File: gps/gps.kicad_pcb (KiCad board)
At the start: 2 copper layers, 38 x 38 mm, 32 parts, among them P1 CTL, P2 PWR, P3 UART, U1 USB_A_FEMALE, U2 TXS0102, U3 SE880, U4 ABS25, U5 TPS76318, U6 SGP25C, U7 KT2520, U8 TPS76333

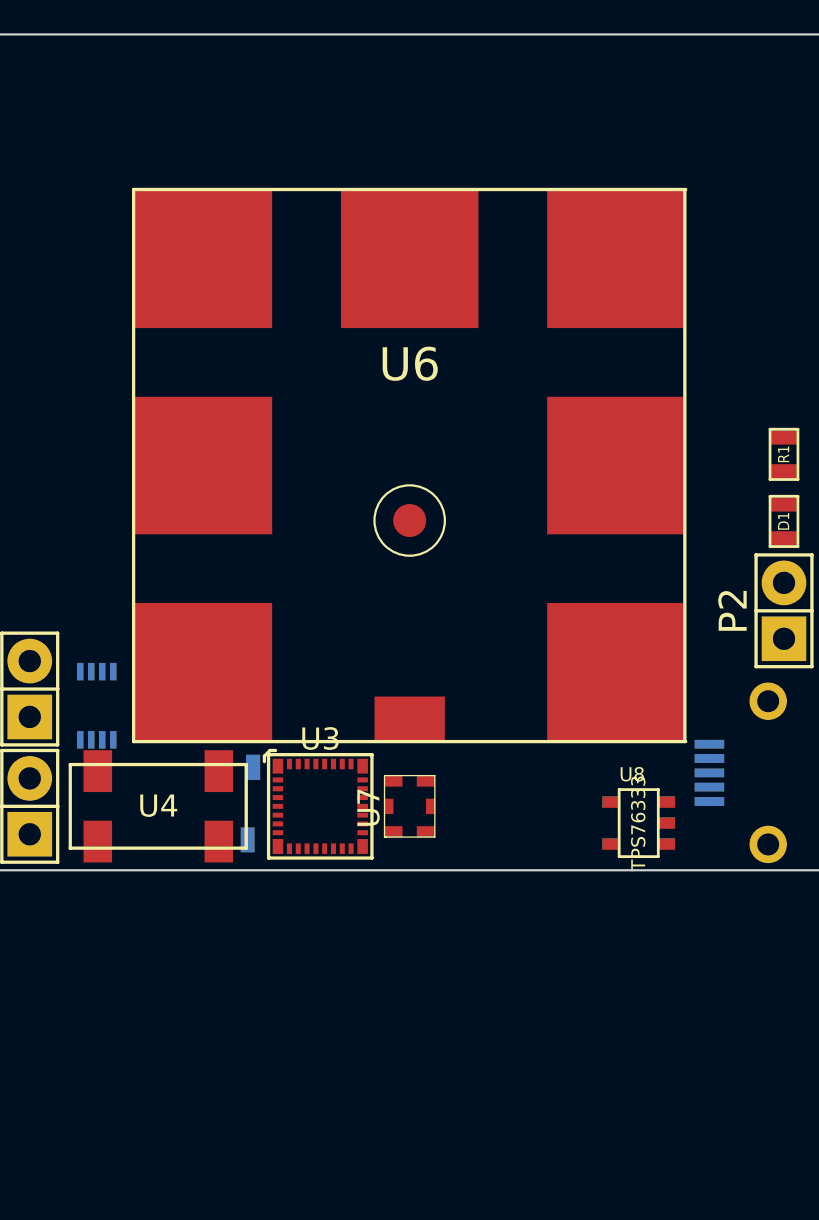
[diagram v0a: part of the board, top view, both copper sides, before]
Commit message: added jumpers to switch communication method
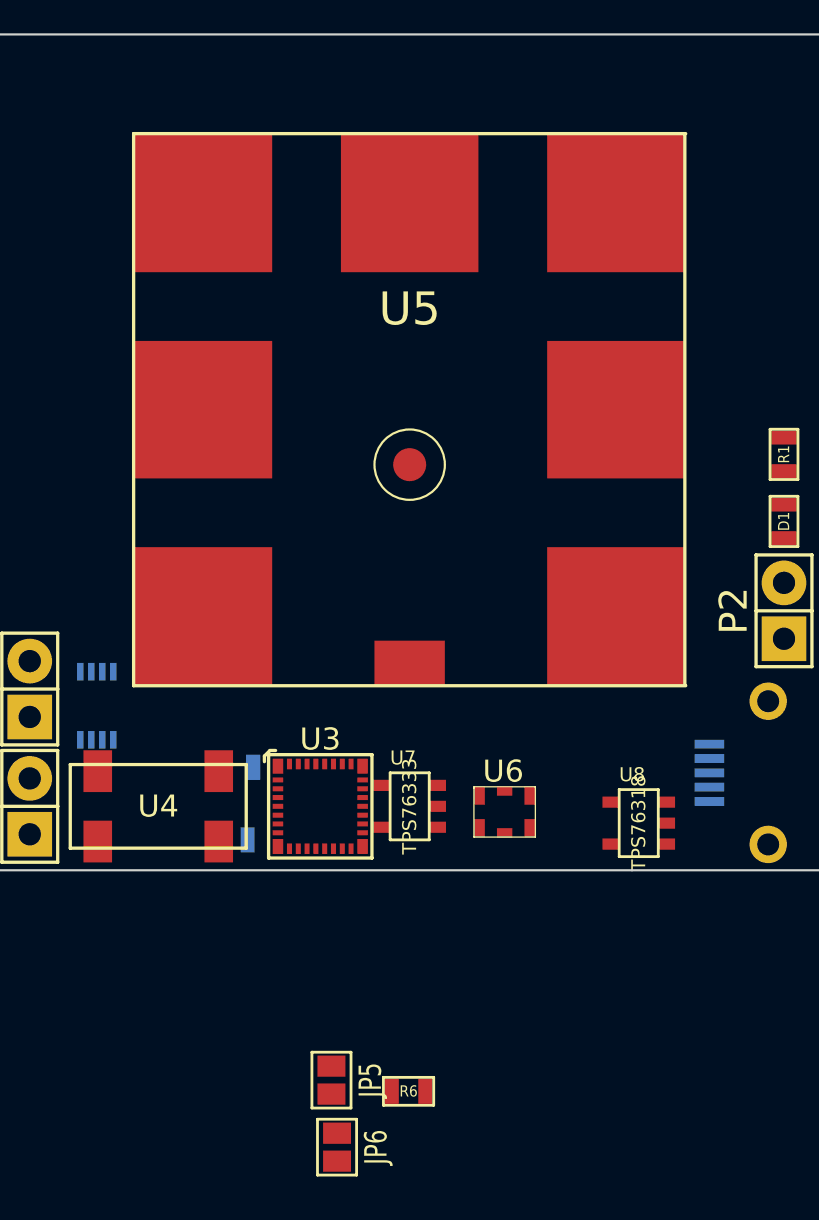
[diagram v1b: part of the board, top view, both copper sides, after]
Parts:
- added JP5: JUMPER, Connect:GS2, F.Cu at (167.9, 78.7)
- added JP6: JUMPER, Connect:GS2, F.Cu at (168.1, 81.8)
- added R6: 6k, SMD_Packages:SMD-0603, F.Cu at (171.4, 79.3)
- C10: value 10uF -> .1uF
- C5: value 1uF -> .1uF
- C6: value .1uF -> 1uF
- C7: value 10uF -> 1uF
- C8: value .1uF -> 10uF
- C9: value 1uF -> 10uF
- P1: value CTL -> PWR
- P2: value PWR -> CTL
- R3: value 10k -> 100k
- R5: value 6k -> 10k
- U5: value TPS76318 -> SGP25C; footprint SMD_Packages:SOT-23-5 -> gps:SGP25C; moved to F.Cu
- U6: value SGP25C -> KT2520; footprint gps:SGP25C -> gps:KT2520
- U7: value KT2520 -> TPS76333; footprint gps:KT2520 -> SMD_Packages:SOT-23-5
- U8: value TPS76333 -> TPS76318
- moved U5 21.5 mm to (171.4, 48.3), turned to 0 degrees
- moved U6 16.3 mm to (175.8, 66.5)
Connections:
- C11 pad 1: 3.3V -> 1.8V
- C5 pad 1: 5V -> Net-(C5-Pad1)
- C6 pad 1: Net-(C6-Pad1) -> 5V
- C7 pad 1: 1.8V -> 5V
- C8 pad 1: 1.8V -> 3.3V
- C9 pad 1: 5V -> 1.8V
- JP1 pad 2: 1.8V -> Net-(JP1-Pad2)
- JP2 pad 1: Net-(JP1-Pad1) -> Net-(JP2-Pad1)
- JP2 pad 2: DGND -> Net-(JP2-Pad2)
- P1 pad 1: ON_OFF -> DGND
- P1 pad 2: SYSTEM_ON -> 5V
- P2 pad 1: DGND -> ON_OFF
- P2 pad 2: 5V -> SYSTEM_ON
- R3 pad 1: Net-(R3-Pad1) -> Net-(JP1-Pad1)
- R3 pad 2: 1.8V -> DGND
- R4 pad 1: Net-(JP1-Pad1) -> 1.8V
- R4 pad 2: Net-(R4-Pad2) -> Net-(JP2-Pad1)
- U3 pad 16: Net-(R5-Pad2) -> Net-(R6-Pad2)
- U3 pad 17: Net-(R4-Pad2) -> Net-(R5-Pad2)
- U3 pad 19: Net-(C6-Pad1) -> Net-(C5-Pad1)
- U3 pad 31: Net-(R3-Pad1) -> Net-(JP2-Pad2)
- U3 pad 32: Net-(U3-Pad32) -> Net-(JP1-Pad2)
- U5 pad 1: 5V -> /50ohm
- U5 pad 3: 5V -> Net-(U5-Pad3)
- U5 pad 5: 1.8V -> Net-(U5-Pad5)
- U6 pad 1: /50ohm -> DGND
- U6 pad 2: DGND -> Net-(U6-Pad2)
- U6 pad 3: Net-(U6-Pad3) -> DGND
- U6 pad 4: Net-(U6-Pad4) -> Net-(U3-Pad21)
- U6 pad 6: Net-(U6-Pad6) -> Net-(C5-Pad1)
- U7 pad 1: DGND -> 5V
- U7 pad 2: Net-(U7-Pad2) -> DGND
- U7 pad 3: DGND -> 5V
- U7 pad 4: Net-(U3-Pad21) -> Net-(U7-Pad4)
- U7 pad 5: Net-(U7-Pad5) -> 3.3V
- U8 pad 5: 3.3V -> 1.8V

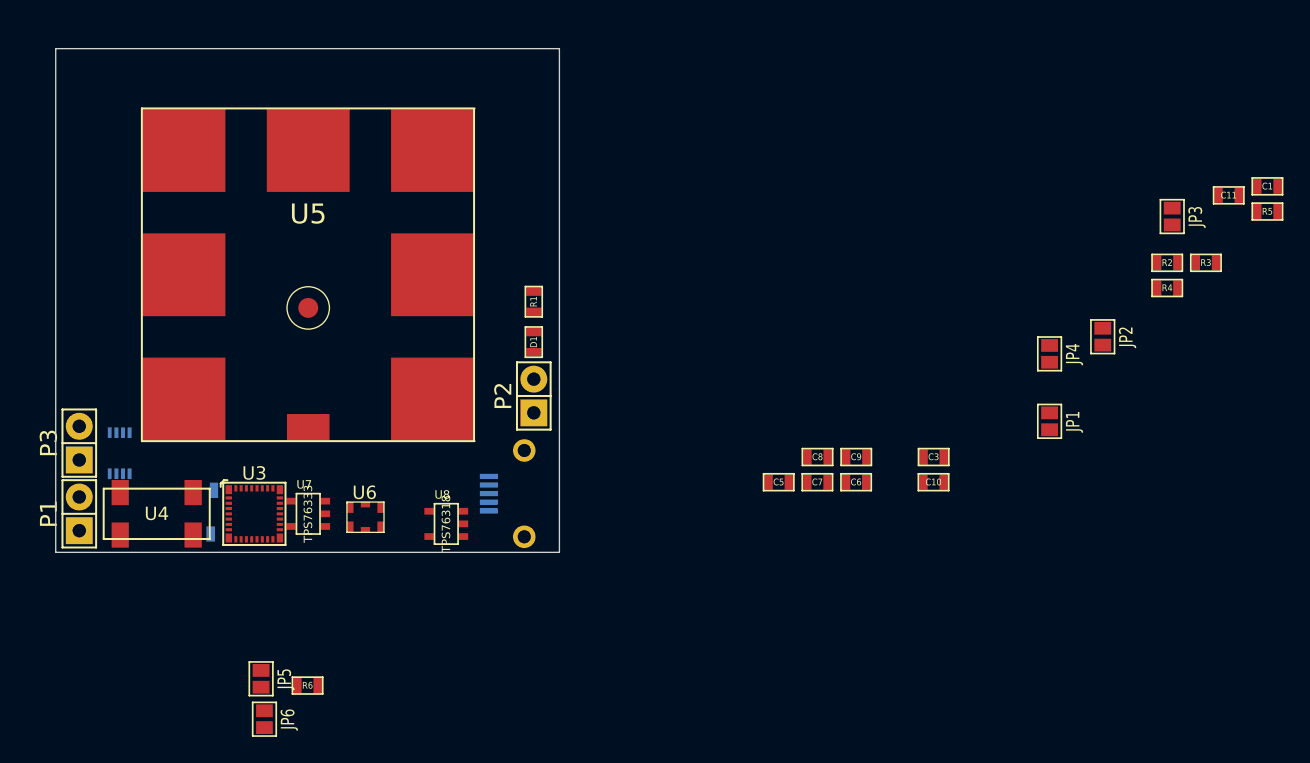
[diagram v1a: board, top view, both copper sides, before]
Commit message: need to place all components on bottom and create analog ground plane for antenna
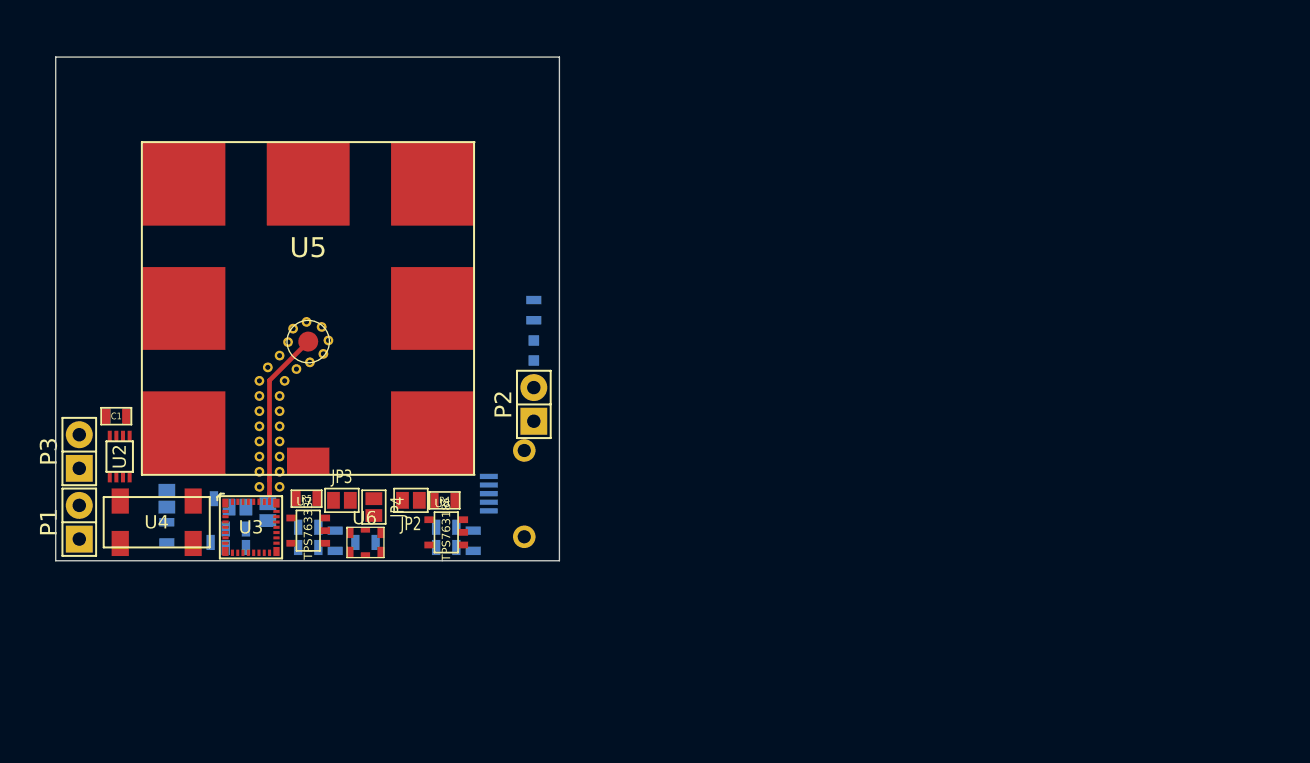
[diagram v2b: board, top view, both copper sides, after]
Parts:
- added ant_via: VAL**, gps:ant_via, F.Cu at (167.8, 56.3)
- added ant_via1: VAL**, gps:ant_via, F.Cu at (167.8, 64.3)
- added ant_via10: VAL**, gps:ant_via, F.Cu at (169.3, 54.4)
- added ant_via11: VAL**, gps:ant_via, F.Cu at (169.9, 53.3)
- added ant_via12: VAL**, gps:ant_via, F.Cu at (170.3, 52.3)
- added ant_via14: VAL**, gps:ant_via, F.Cu at (171.3, 51.8)
- added ant_via15: VAL**, gps:ant_via, F.Cu at (172.5, 52.2)
- added ant_via16: VAL**, gps:ant_via, F.Cu at (173.0, 53.2)
- added ant_via17: VAL**, gps:ant_via, F.Cu at (172.6, 54.2)
- added ant_via18: VAL**, gps:ant_via, F.Cu at (171.6, 54.9)
- added ant_via19: VAL**, gps:ant_via, F.Cu at (170.6, 55.4)
- added ant_via2: VAL**, gps:ant_via, F.Cu at (167.8, 63.1)
- added ant_via20: VAL**, gps:ant_via, F.Cu at (169.7, 56.3)
- added ant_via21: VAL**, gps:ant_via, F.Cu at (169.3, 57.4)
- added ant_via22: VAL**, gps:ant_via, F.Cu at (169.3, 58.5)
- added ant_via23: VAL**, gps:ant_via, F.Cu at (169.3, 59.7)
- added ant_via24: VAL**, gps:ant_via, F.Cu at (169.3, 60.8)
- added ant_via25: VAL**, gps:ant_via, F.Cu at (169.3, 62.0)
- added ant_via26: VAL**, gps:ant_via, F.Cu at (169.3, 63.1)
- added ant_via27: VAL**, gps:ant_via, F.Cu at (169.3, 64.3)
- added ant_via3: VAL**, gps:ant_via, F.Cu at (167.8, 62.0)
- added ant_via4: VAL**, gps:ant_via, F.Cu at (167.8, 60.8)
- added ant_via5: VAL**, gps:ant_via, F.Cu at (167.8, 59.7)
- added ant_via7: VAL**, gps:ant_via, F.Cu at (167.8, 58.5)
- added ant_via8: VAL**, gps:ant_via, F.Cu at (167.8, 57.4)
- added ant_via9: VAL**, gps:ant_via, F.Cu at (168.4, 55.2)
- C10, C11, C3, C5, C6, C7, C8, C9, JP1, JP5, JP6, R1, R2, R3, R6: moved to B.Cu
- D1: footprint SMD_Packages:SMD-0603 -> LEDs:LED-0603; moved to B.Cu
- U2: moved to F.Cu
- moved C1 88.6 mm to (157.0, 58.9), turned to 180 degrees
- moved R3 81.0 mm to (160.8, 67.7), turned to 270 degrees
- moved R5 75.7 mm to (171.3, 65.2), turned to 180 degrees
- moved R2 73.5 mm to (166.0, 68.8), turned to 180 degrees
- moved JP1 66.9 mm to (160.8, 65.2)
- moved JP3 66.2 mm to (174.0, 65.3), turned to 90 degrees
- moved C11 64.1 mm to (181.9, 67.3)
- moved C3 61.7 mm to (157.0, 58.9)
- moved R4 56.8 mm to (181.7, 65.3), turned to 180 degrees
- moved JP2 53.6 mm to (179.2, 65.3), turned to 270 degrees
- moved JP4 52.3 mm to (176.4, 65.8)
- moved C10 47.3 mm to (171.4, 67.3)
- moved C6 39.5 mm to (173.5, 68.3), turned to 270 degrees
- moved C8 39.0 mm to (171.4, 68.8)
- moved C9 31.7 mm to (181.9, 68.8)
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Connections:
- U3 pad 23: DGND -> AGND
- U3 pad 24: DGND -> AGND
- U3 pad 25: DGND -> AGND
- U3 pad 26: DGND -> AGND
- U3 pad 28: DGND -> AGND
- U3 pad 29: DGND -> AGND
- U5 pad 2: DGND -> AGND
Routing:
- net /50ohm: track 0.00 -> 13.3 mm
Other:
- net class Default: clearance 0.254 -> 0.1524; trace_width 0.254 -> 0.1524; via_dia 0.889 -> 0.7366; via_drill 0.635 -> 0.381
- net class ohm added: clearance 0.1524, trace_width 0.3556, via_dia 0.7366, via_drill 0.381
- rule trace_clearance: 0.254 -> 0.1524
- rule trace_min: 0.254 -> 0.1524
- rule via_min_drill: 0.508 -> 0.381
- rule via_min_size: 0.889 -> 0.7366

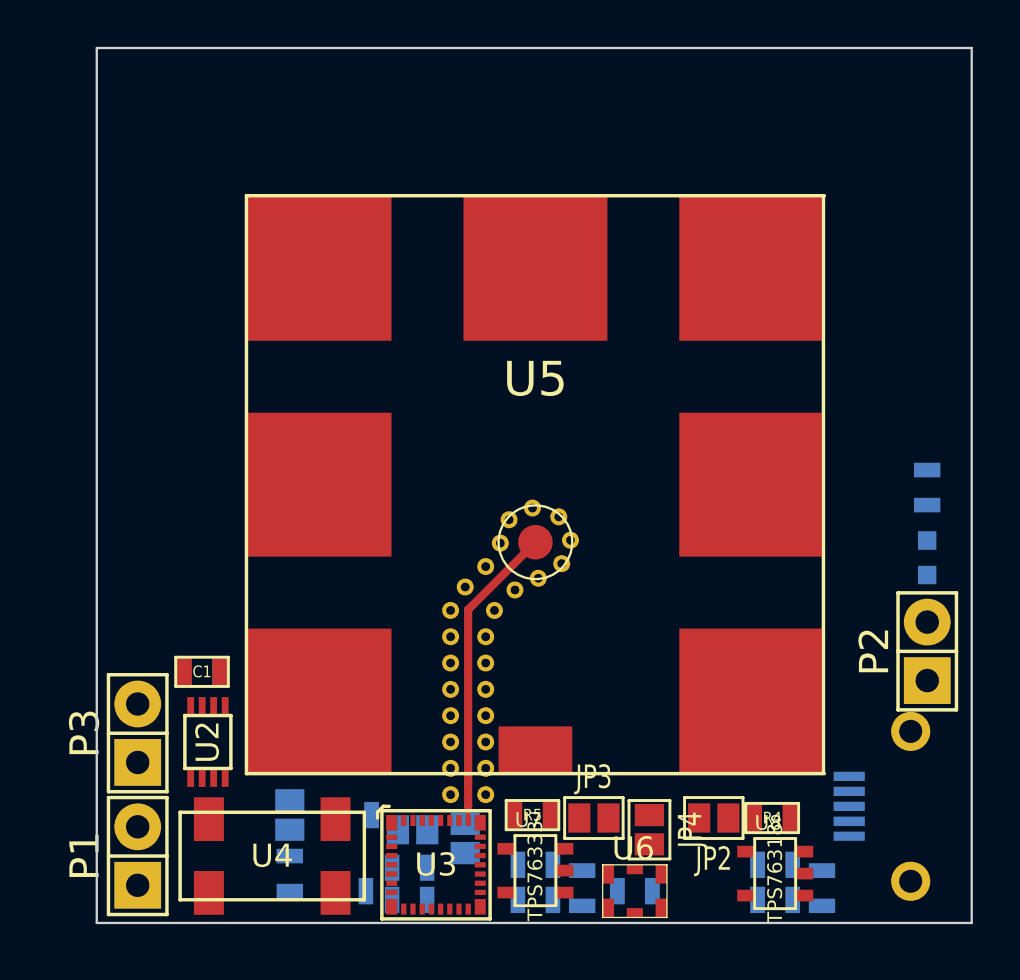
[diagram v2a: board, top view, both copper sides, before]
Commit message: modeled the 50ohm trace as grounded coplanar. need to move things around better so it can solve
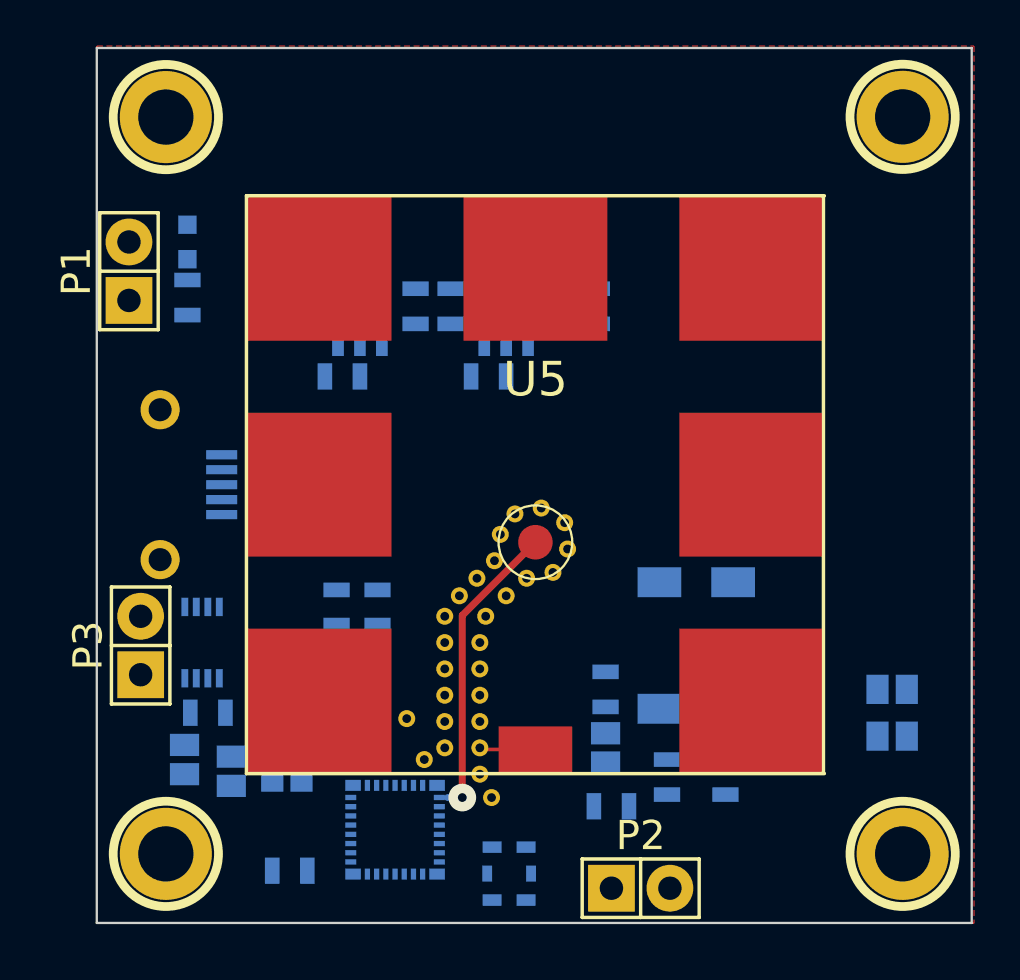
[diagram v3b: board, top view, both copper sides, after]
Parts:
- added 1PIN: P***, Connect:1pin, F.Cu at (155.4, 34.8)
- added 2PIN: P***, Connect:1pin, F.Cu at (187.4, 34.8)
- added 3PIN: P***, Connect:1pin, F.Cu at (187.4, 66.8)
- added 4PIN: P***, Connect:1pin, F.Cu at (155.4, 66.8)
- added ant_via10: VAL**, gps:ant_via, F.Cu at (169.7, 54.1)
- C1, JP2, JP3, JP4, R4, R5, U2, U3, U4, U6, U7, U8: moved to B.Cu
- moved U1 40.6 mm to (152.4, 50.8), turned to 90 degrees
- moved D1 34.9 mm to (156.3, 40.3)
- moved R1 33.2 mm to (156.3, 42.7)
- moved C9 27.4 mm to (172.6, 43.1), turned to 270 degrees
- moved U8 26.8 mm to (170.2, 43.6), turned to 180 degrees
- moved C7 26.5 mm to (169.4, 46.1), turned to 0 degrees
- moved C8 26.3 mm to (166.2, 43.1), turned to 270 degrees
- moved C11 25.5 mm to (174.1, 43.1), turned to 270 degrees
- moved P1 25.4 mm to (153.8, 41.5)
- moved U7 25.2 mm to (163.8, 43.6), turned to 180 degrees
- moved C6 24.5 mm to (163.1, 46.1), turned to 0 degrees
- moved C10 24.5 mm to (167.8, 43.1), turned to 270 degrees
- moved R4 21.4 mm to (160.7, 61.6), turned to 0 degrees
- moved JP6 21.2 mm to (186.9, 61.7)
- moved U4 20.6 mm to (178.4, 57.8), turned to 90 degrees
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- renumbered ant_via10 to ant_via28
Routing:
- net AGND: track 0.00 -> 2.44 mm
- net /50ohm: track 13.3 -> 13.4 mm, vias 0 -> 1
- added copper zone on F.Cu, net (none)
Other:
- net class ohm: trace_width 0.3556 -> 0.3048; via_dia 0.7366 -> 1.20142
- rule pad_to_mask_clearance: 0 -> 0.0508
